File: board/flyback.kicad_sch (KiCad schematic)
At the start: 23 parts, among them U1 MP8007, U2 POE13P-50L

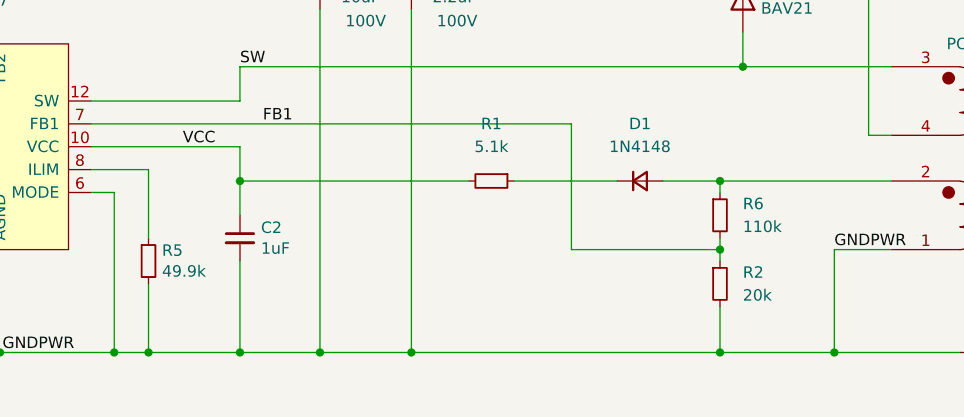
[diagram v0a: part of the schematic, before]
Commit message: updated voltage and current setting resistors
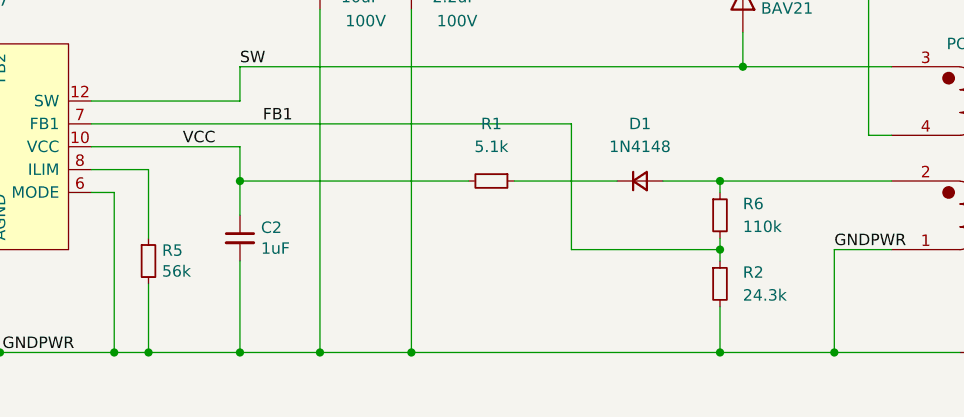
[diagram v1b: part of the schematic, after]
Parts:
- R2: value 20k -> 24.3k
- R5: value 49.9k -> 56k
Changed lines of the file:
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@@
       (effects (font (size 1.27 1.27)) (justify left))
     )
-    (property "Value" "49.9k" (id 1) (at 123.4186 104.013 0)
+    (property "Value" "56k" (id 1) (at 123.4186 104.013 0)
       (effects (font (size 1.27 1.27)) (justify left))
     )
@@
       (effects (font (size 1.27 1.27)) (justify left))
     )
-    (property "Value" "20k" (id 1) (at 187.96 106.6799 0)
+    (property "Value" "24.3k" (id 1) (at 187.96 106.6799 0)
       (effects (font (size 1.27 1.27)) (justify left))
     )
